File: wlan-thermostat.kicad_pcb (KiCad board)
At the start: 2 copper layers, 0 parts

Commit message: Updated template for KiCAD 7
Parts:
- added G***: LOGO, Chof747 Logos:LOGO small, F.Cu at (108.8, 93.5)

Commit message: Initial board version
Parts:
- added C1: 1uF, Capacitor_SMD:C_0603_1608Metric_Pad1.08x0.95mm_HandSolder, F.Cu at (97.2, 68.9)
- added C2: 1uF, Capacitor_SMD:C_0603_1608Metric_Pad1.08x0.95mm_HandSolder, F.Cu at (103.8, 68.9)
- added C3: 10uF, Capacitor_SMD:C_0603_1608Metric_Pad1.08x0.95mm_HandSolder, F.Cu at (108.4, 62.2)
- added F1: Fuse, Fuse:Fuse_1206_3216Metric_Pad1.42x1.75mm_HandSolder, F.Cu at (146.2, 73.7)
- added H1: MountingHole, MountingHole:MountingHole_3.2mm_M3, F.Cu at (97.4, 40.3)
- added H2: MountingHole, MountingHole:MountingHole_3.2mm_M3, F.Cu at (151.9, 76.1)
- added IC1: ME6211C33M5G-N, Chof747 Footprints:SOT95P270X145-5N, F.Cu at (100.5, 68.9)
- added J1: PROG_HDR, Connector_PinHeader_2.54mm:PinHeader_1x06_P2.54mm_Vertical, F.Cu at (111.8, 77.5)
- added J2: Conn_01x02, Connector_PinHeader_2.54mm:PinHeader_1x02_P2.54mm_Vertical, B.Cu at (105.9, 59.2)
- added J3: Conn_01x02, Connector_PinHeader_2.54mm:PinHeader_1x02_P2.54mm_Vertical, B.Cu at (133.1, 59.2)
- added JP1: PWR_PROG, Connector_PinHeader_2.54mm:PinHeader_1x02_P2.54mm_Vertical, F.Cu at (143.0, 72.4)
- added Q1: SS8050-G, Package_TO_SOT_SMD:SOT-23, F.Cu at (134.0, 72.5)
- added Q2: SS8050-G, Package_TO_SOT_SMD:SOT-23, F.Cu at (138.4, 72.5)
- added R1: 10k, Resistor_SMD:R_0603_1608Metric_Pad0.98x0.95mm_HandSolder, F.Cu at (133.0, 77.1)
- added R10: 10k, Resistor_SMD:R_0603_1608Metric_Pad0.98x0.95mm_HandSolder, F.Cu at (97.5, 61.3)
- added R2: 10k, Resistor_SMD:R_0603_1608Metric_Pad0.98x0.95mm_HandSolder, F.Cu at (135.5, 77.1)
- added R3: 1k, Resistor_SMD:R_0603_1608Metric_Pad0.98x0.95mm_HandSolder, F.Cu at (146.3, 47.6)
- added R4: 1k, Resistor_SMD:R_0603_1608Metric_Pad0.98x0.95mm_HandSolder, F.Cu at (140.2, 47.6)
- added R5: 22k, Resistor_SMD:R_0603_1608Metric_Pad0.98x0.95mm_HandSolder, F.Cu at (148.1, 47.6)
- added R6: 22k, Resistor_SMD:R_0603_1608Metric_Pad0.98x0.95mm_HandSolder, F.Cu at (142.0, 47.6)
- added R7: 10k, Resistor_SMD:R_0603_1608Metric_Pad0.98x0.95mm_HandSolder, F.Cu at (106.8, 52.9)
- added R8: 10k, Resistor_SMD:R_0603_1608Metric_Pad0.98x0.95mm_HandSolder, F.Cu at (108.7, 52.9)
- added R9: 10k, Resistor_SMD:R_0603_1608Metric_Pad0.98x0.95mm_HandSolder, F.Cu at (97.5, 59.7)
- added SW1: SW_Push, Button_Switch_THT:SW_PUSH_6mm, F.Cu at (97.1, 48.3)
- added SW2: RotaryEncoder_Switch, Chof747 Footprints:PEC12R3120FS0012, F.Cu at (146.6, 66.0)
- added U1: ESP-12F, RF_Module:ESP-12E, F.Cu at (118.7, 50.8)
- added U2: SHT4x, Sensor_Humidity:Sensirion_DFN-4_1.5x1.5mm_P0.8mm_SHT4x_NoCentralPad, F.Cu at (149.2, 39.8)
- added U3: SSD1306, Chof747 Footprints:AZ Delivery SS1306 OLED, F.Cu at (118.7, 59.0)
- G***: footprint Chof747 Logos:LOGO small -> Chof747 Logos:LOGO large; moved to B.Cu
- moved G*** 32.9 mm to (111.6, 60.7), turned to 180 degrees
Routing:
- net GPIO5_SCL: track 0.00 -> 145.7 mm, vias 0 -> 6
- net GPIO4_SDA: track 0.00 -> 131.8 mm, vias 0 -> 2
- net +3V3: track 0.00 -> 131.7 mm, vias 0 -> 4
- net ~{RESET}: track 0.00 -> 121.0 mm, vias 0 -> 2
- net ~{GPIO0}: track 0.00 -> 39.9 mm, vias 0 -> 2
- net GPIO14_RENCLK: track 0.00 -> 39.8 mm
- net GPIO3_RX: track 0.00 -> 37.9 mm
- net GPIO13_RENBTN: track 0.00 -> 37.4 mm, vias 0 -> 2
- net /3v3PROG: track 0.00 -> 37.1 mm
- net GPIO4_TX: track 0.00 -> 35.3 mm
- net GPIO12_RENDAT: track 0.00 -> 33.9 mm
- net DTR: track 0.00 -> 20.9 mm
- net GPIO15_RELAY: track 0.00 -> 20.7 mm
- net RTS: track 0.00 -> 20.5 mm
- net +5V: track 0.00 -> 19.0 mm
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- added copper zone on B.Cu, net GND
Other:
- board outline added: 62.4 x 43.5 mm
- board text added: "3V3"
- board text added: "5V"
- board text added: "DTR"
- board text added: "G"
- board text added: "GND"
- board text added: "REL"
- board text added: "RTS"
- board text added: "RX"
- board text added: "TX"
- board text added: "WLAN Thermostat Frontpanel v1.0 (2023)"

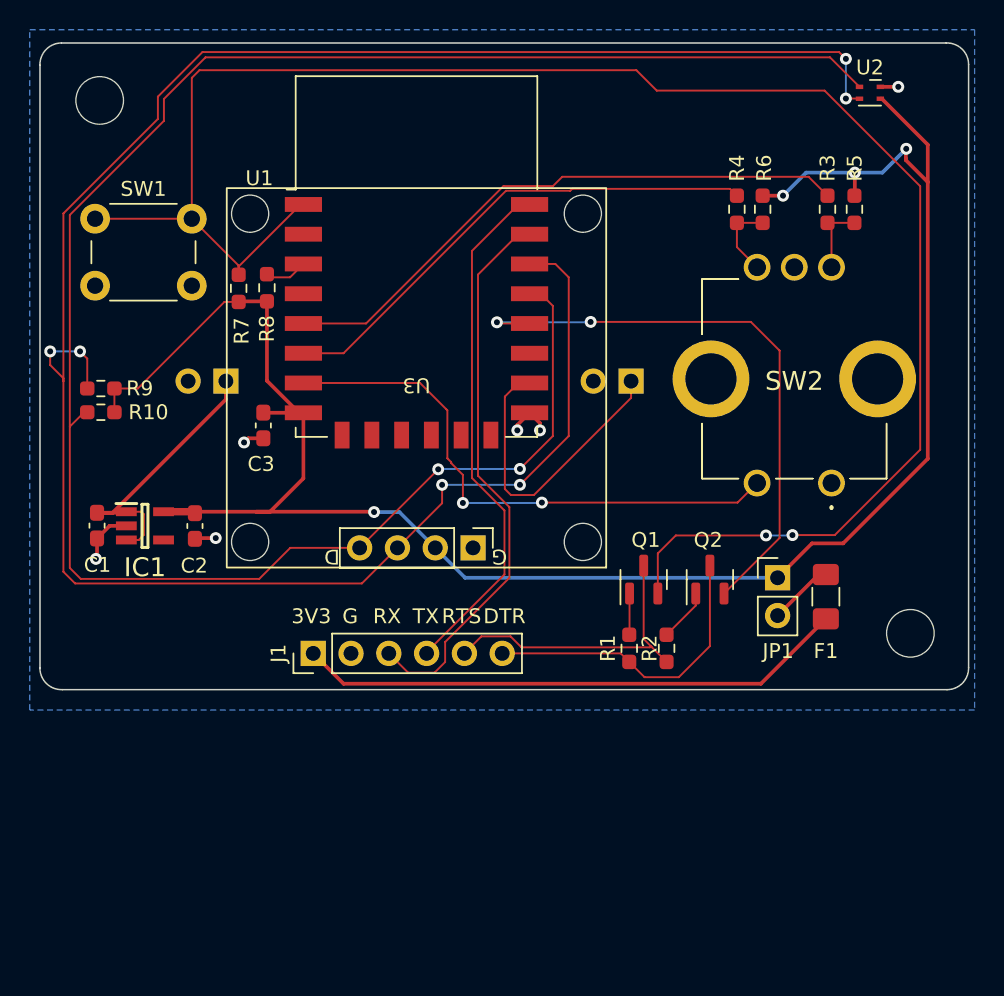
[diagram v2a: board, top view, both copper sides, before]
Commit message: Changed board size to fit into standard frame for power outlet
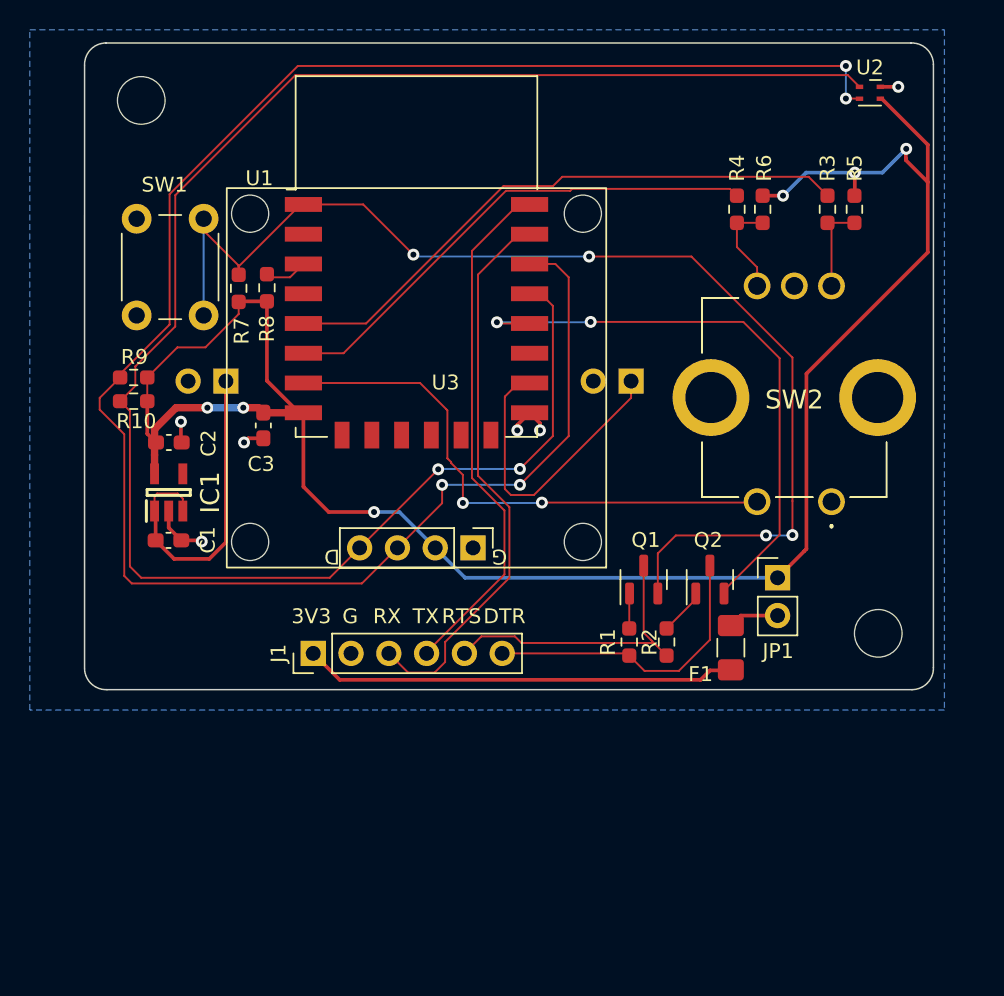
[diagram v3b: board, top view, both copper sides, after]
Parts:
- moved SW1 7.29 mm to (104.4, 48.3), turned to -90 degrees
- moved F1 7.25 mm to (139.8, 77.1)
- moved C2 5.88 mm to (102.1, 63.3), turned to 0 degrees
- moved C1 4.90 mm to (102.0, 69.9), turned to 0 degrees
- moved H1 2.79 mm to (100.2, 40.3)
- moved IC1 2.75 mm to (102.0, 66.7), turned to 90 degrees
- moved R10 2.33 mm to (99.7, 60.5)
- moved R9 2.33 mm to (99.7, 58.9)
- moved H2 2.16 mm to (149.7, 76.1)
- moved SW2 1.25 mm to (146.6, 67.3)
- moved R1 0.42 mm to (133.0, 76.7)
- moved R2 0.42 mm to (135.5, 76.7)
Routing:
- net ~{RESET}: track 121.0 -> 79.5 mm, vias 2 -> 4
- net GPIO5_SCL: track 145.7 -> 129.0 mm, vias 6 -> 4
- net GPIO4_SDA: track 131.8 -> 119.7 mm
- net /3v3PROG: track 37.1 -> 29.1 mm
- net +5V: track 19.0 -> 22.5 mm
- net +3V3: track 131.7 -> 130.2 mm, vias 4 -> 6
- net Net-(SW2-CHANNEL_B): track 5.28 -> 6.53 mm
- net Net-(SW2-CHANNEL_A): track 4.91 -> 6.16 mm
- net /3v3PROG_SAVE: track 4.38 -> 3.42 mm
- net DTR: track 20.9 -> 20.3 mm
- net GPIO13_RENBTN: track 37.4 -> 36.9 mm
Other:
- board size 62.4 x 43.5 mm -> 57 x 43.5 mm
